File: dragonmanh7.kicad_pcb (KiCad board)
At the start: 4 copper layers, 135.6 x 54.6 mm, 109 parts, among them J1 USB_B, J10 Conn_02x12_Odd_Even, J11 Conn_02x03_Odd_Even, J12 VBAT+, J13 Conn_02x05_Odd_Even, J14 VBATG, J15 Conn_02x02_Odd_Even, J18 Conn_02x05_Odd_Even, J2 73725-0110BLF, J3 RJ45_Amphenol_RJMG1BD3B8K1ANR, J4 Micro_SD_Card, J5 Screw_Terminal_01x06, J6 Conn_02x12_Odd_Even, J7 USB_B, J8 Screw_Terminal_01x02, J9 Conn_02x12_Odd_Even, SW1 RESET, SW2 PC13, U1 STM32H743VITx, U10 USBLC6-2SC6, U11 SN6505, U12 TCAN332, U13 ISL83483, U14 MIC2005A, U2 KSZ8081RNA, U3 ISO1050DUB, U4 ISO3082DW, U5 S25FL127SABMFI101, U6 AP63203, U7 USBLC6-2SC6, U8 STM32F042F6Px, U9 USBLC6-2SC6, Y1 8MHz, Y2 32.768KHz, Y3 25MHz

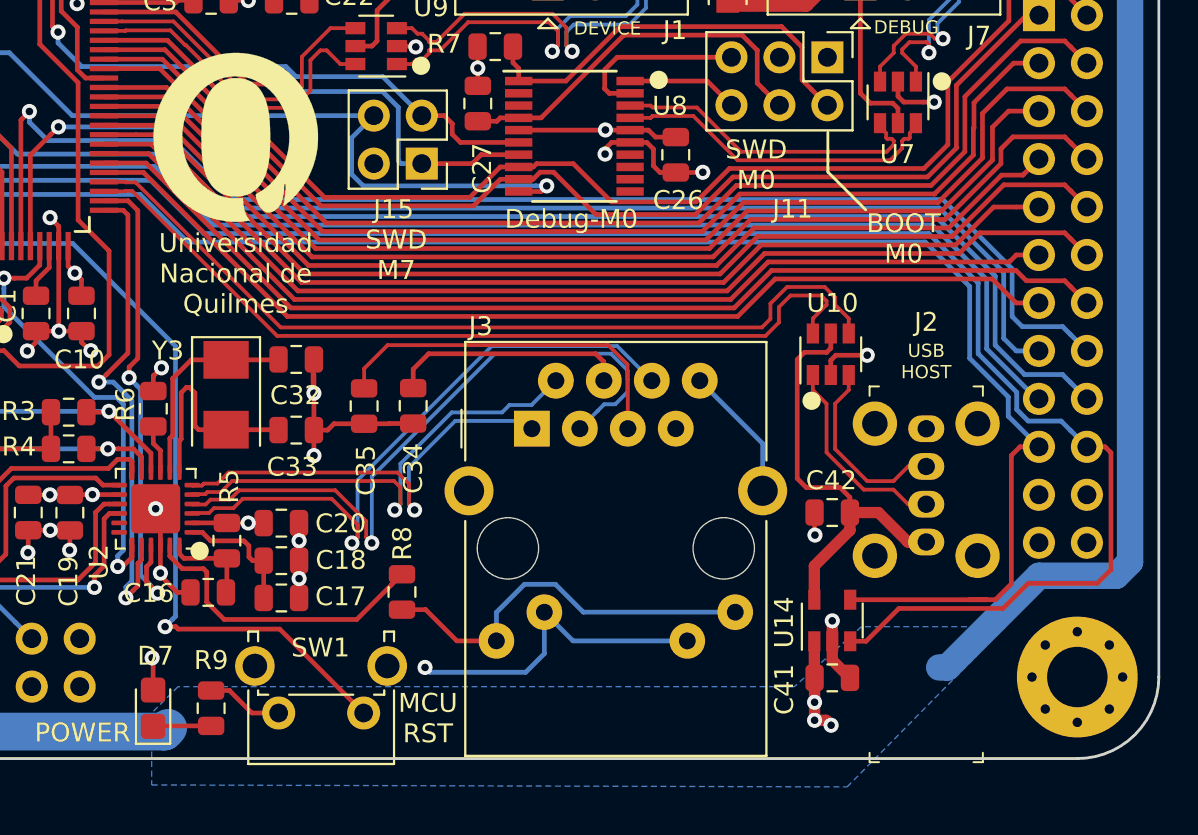
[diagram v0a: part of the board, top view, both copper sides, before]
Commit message: Reroute the power plane above RJ45 to prevent coupling
Signed-off-by: Martin Ribelotta <martinribelotta@gmail.com>
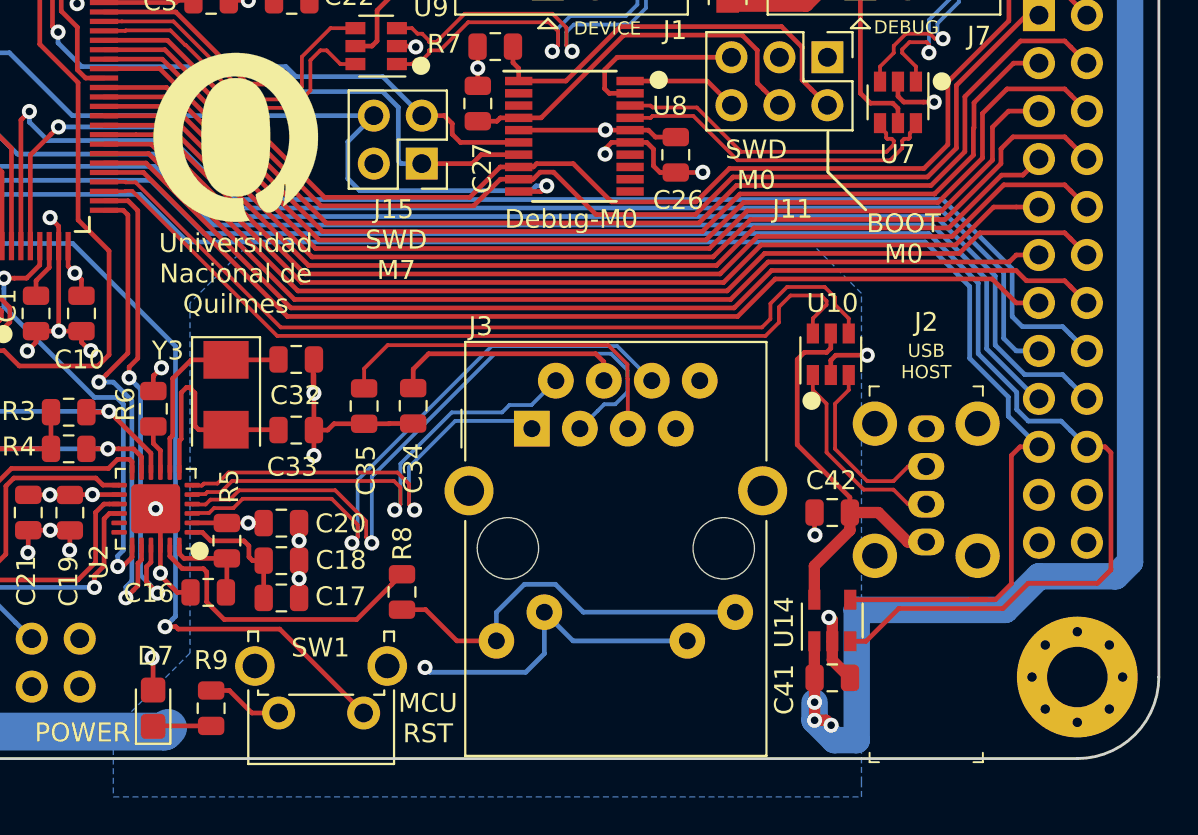
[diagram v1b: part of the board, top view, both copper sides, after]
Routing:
- net VDC: track 151.9 -> 165.6 mm
- net GND: track 178.7 -> 171.8 mm
- net /VBUS3: track 23.2 -> 22.2 mm
- net /~RESET: track 135.6 -> 136.2 mm
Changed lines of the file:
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@@
     (thickness 1.6)
     (drawings 76)
-    (tracks 2290)
+    (tracks 2293)
     (zones 0)
     (modules 109)
@@
   (segment (start 177.01514 77.33768) (end 177.95264 78.27518) (width 0.6) (layer F.Cu) (net 2))
   (segment (start 177.01514 76.33734) (end 177.01514 77.33768) (width 0.6) (layer F.Cu) (net 2))
-  (via (at 177.01514 75.25512) (size 0.8) (drill 0.4) (layers F.Cu B.Cu) (net 2))
-  (segment (start 177.01514 76.33734) (end 177.01514 75.25512) (width 0.6) (layer F.Cu) (net 2))
   (segment (start 109.22 33.0985) (end 109.22 33.02) (width 0.25) (layer F.Cu) (net 2))
   (segment (start 111.76 35.6385) (end 109.22 33.0985) (width 0.25) (layer F.Cu) (net 2))
@@
   (segment (start 163.28712 76.31734) (end 169.33712 76.31734) (width 0.25) (layer B.Cu) (net 2))
   (segment (start 161.76712 74.79734) (end 163.28712 76.31734) (width 0.25) (layer B.Cu) (net 2))
-  (segment (start 173.32712 65.86734) (end 173.32712 68.36734) (width 0.25) (layer B.Cu) (net 2))
-  (segment (start 169.99712 62.53734) (end 173.32712 65.86734) (width 0.25) (layer B.Cu) (net 2))
   (via (at 155.448 77.724) (size 0.8) (drill 0.4) (layers F.Cu B.Cu) (net 2))
   (segment (start 155.702 77.978) (end 155.448 77.724) (width 0.25) (layer B.Cu) (net 2))
@@
   (segment (start 150.28926 65.15354) (end 149.56306 65.15354) (width 0.25) (layer F.Cu) (net 2))
   (segment (start 150.6243 64.8185) (end 150.28926 65.15354) (width 0.25) (layer F.Cu) (net 2))
+  (segment (start 176.881544 75.073744) (end 176.833764 75.073744) (width 0.6) (layer F.Cu) (net 2))
+  (segment (start 177.01514 76.33734) (end 177.01514 75.20734) (width 0.6) (layer F.Cu) (net 2))
+  (via (at 176.833764 75.073744) (size 0.8) (drill 0.4) (layers F.Cu B.Cu) (net 2))
+  (segment (start 177.01514 75.20734) (end 176.881544 75.073744) (width 0.6) (layer F.Cu) (net 2))
   (segment (start 134.84606 57.245772) (end 134.84606 58.03876) (width 0.25) (layer F.Cu) (net 3))
   (segment (start 135.545281 55.410141) (end 135.545281 56.546551) (width 0.25) (layer F.Cu) (net 3))
@@
   (segment (start 125.73762 49.90592) (end 131.1021 55.2704) (width 0.25) (layer B.Cu) (net 33))
   (segment (start 160.40756 52.5185) (end 161.593396 52.5185) (width 0.25) (layer F.Cu) (net 33))
-  (segment (start 151.560279 51.605301) (end 152.174113 52.219135) (width 0.25) (layer B.Cu) (net 33))
   (via (at 161.892761 52.219135) (size 0.8) (drill 0.4) (layers F.Cu B.Cu) (net 33))
-  (segment (start 152.174113 52.219135) (end 161.327076 52.219135) (width 0.25) (layer B.Cu) (net 33))
   (segment (start 161.593396 52.5185) (end 161.892761 52.219135) (width 0.25) (layer F.Cu) (net 33))
-  (segment (start 151.560279 49.676301) (end 151.560279 51.605301) (width 0.25) (layer B.Cu) (net 33))
-  (segment (start 152.73528 48.5013) (end 151.560279 49.676301) (width 0.25) (layer B.Cu) (net 33))
   (segment (start 161.327076 52.219135) (end 161.892761 52.219135) (width 0.25) (layer B.Cu) (net 33))
+  (segment (start 161.069811 52.4764) (end 161.327076 52.219135) (width 0.25) (layer B.Cu) (net 33))
+  (segment (start 151.9936 52.4764) (end 161.069811 52.4764) (width 0.25) (layer B.Cu) (net 33))
+  (segment (start 151.3586 51.8414) (end 151.9936 52.4764) (width 0.25) (layer B.Cu) (net 33))
+  (segment (start 152.73528 48.5013) (end 151.3586 49.87798) (width 0.25) (layer B.Cu) (net 33))
+  (segment (start 151.3586 49.87798) (end 151.3586 51.8414) (width 0.25) (layer B.Cu) (net 33))
   (segment (start 130.19532 64.94018) (end 130.72364 64.41186) (width 0.25) (layer F.Cu) (net 34))
   (segment (start 129.667 64.94018) (end 130.19532 64.94018) (width 0.25) (layer F.Cu) (net 34))
@@
   (segment (start 107.739978 81.11998) (end 107.00766 80.387662) (width 2) (layer B.Cu) (net 46))
   (segment (start 105.239701 73.997701) (end 98.381701 73.997701) (width 2) (layer B.Cu) (net 46))
-  (segment (start 184.404 40.132) (end 180.90642 36.63442) (width 1.4) (layer B.Cu) (net 46))
-  (segment (start 183.1086 77.724) (end 187.962599 72.870001) (width 1.4) (layer B.Cu) (net 46))
-  (segment (start 182.6768 77.724) (end 183.1086 77.724) (width 1.4) (layer B.Cu) (net 46))
+  (segment (start 176.07764 79.56828) (end 176.07764 80.52284) (width 1.4) (layer B.Cu) (net 46))
   (segment (start 191.77 40.132) (end 184.404 40.132) (width 1.4) (layer B.Cu) (net 46))
+  (segment (start 184.404 40.132) (end 180.90642 36.63442) (width 1.4) (layer B.Cu) (net 46))
   (segment (start 192.786 41.148) (end 191.77 40.132) (width 1.4) (layer B.Cu) (net 46))
   (segment (start 192.786 72.136) (end 192.786 41.148) (width 1.4) (layer B.Cu) (net 46))
-  (segment (start 187.962599 72.870001) (end 192.051999 72.870001) (width 1.4) (layer B.Cu) (net 46))
-  (segment (start 192.051999 72.870001) (end 192.786 72.136) (width 1.4) (layer B.Cu) (net 46))
+  (segment (start 192.024 72.898) (end 192.786 72.136) (width 1.4) (layer B.Cu) (net 46))
+  (segment (start 178.308 74.676) (end 186.182 74.676) (width 1.4) (layer B.Cu) (net 46))
+  (segment (start 177.12979 81.57499) (end 178.308 81.57499) (width 1.4) (layer B.Cu) (net 46))
+  (segment (start 176.07764 80.52284) (end 177.12979 81.57499) (width 1.4) (layer B.Cu) (net 46))
+  (segment (start 178.308 81.57499) (end 178.308 74.676) (width 1.4) (layer B.Cu) (net 46))
+  (segment (start 186.182 74.676) (end 187.96 72.898) (width 1.4) (layer B.Cu) (net 46))
+  (segment (start 187.96 72.898) (end 192.024 72.898) (width 1.4) (layer B.Cu) (net 46))
   (segment (start 72.92848 70.83552) (end 73.05954 70.83552) (width 1) (layer F.Cu) (net 47))
   (segment (start 70.60184 74.59182) (end 70.60184 73.16216) (width 1) (layer F.Cu) (net 47))
@@
   (segment (start 176.06514 72.34686) (end 177.9501 70.4619) (width 0.6) (layer F.Cu) (net 62))
   (segment (start 176.9364 60.8178) (end 176.9364 60.0378) (width 0.25) (layer F.Cu) (net 62))
-  (segment (start 175.5394 61.0362) (end 176.718 61.0362) (width 0.25) (layer F.Cu) (net 62))
-  (segment (start 177.9501 69.5198) (end 177.9501 68.7198) (width 0.25) (layer F.Cu) (net 62))
-  (segment (start 177.4293 68.199) (end 175.641 68.199) (width 0.25) (layer F.Cu) (net 62))
-  (segment (start 177.9501 68.7198) (end 177.4293 68.199) (width 0.25) (layer F.Cu) (net 62))
-  (segment (start 175.1584 67.7164) (end 175.1584 61.4172) (width 0.25) (layer F.Cu) (net 62))
   (segment (start 176.718 61.0362) (end 176.9364 60.8178) (width 0.25) (layer F.Cu) (net 62))
-  (segment (start 175.641 68.199) (end 175.1584 67.7164) (width 0.25) (layer F.Cu) (net 62))
+  (segment (start 177.9501 69.5198) (end 177.9501 68.7198) (width 0.25) (layer F.Cu) (net 62))
+  (segment (start 175.1584 65.9281) (end 175.1584 61.4172) (width 0.25) (layer F.Cu) (net 62))
   (segment (start 175.1584 61.4172) (end 175.5394 61.0362) (width 0.25) (layer F.Cu) (net 62))
+  (segment (start 177.9501 68.7198) (end 175.1584 65.9281) (width 0.25) (layer F.Cu) (net 62))
+  (segment (start 175.5394 61.0362) (end 176.718 61.0362) (width 0.25) (layer F.Cu) (net 62))
   (segment (start 180.49494 48.11772) (end 180.21812 47.8409) (width 0.25) (layer F.Cu) (net 63))
   (segment (start 180.49494 48.89772) (end 180.49494 48.11772) (width 0.25) (layer F.Cu) (net 63))
@@
     )
   )
-  (zone (net 46) (net_name VDC) (layer B.Cu) (hatch edge 0.508)
-    (connect_pads (clearance 0.254))
-    (min_thickness 0.254)
-    (fill yes (arc_segments 16) (thermal_gap 0.508) (thermal_bridge_width 0.508))
-    (polygon
-      (pts
-        (xy 140.972535 83.947) (xy 177.8 84.05114) (xy 186.182 75.565) (xy 178.562 75.565) (xy 175.006 78.74)
-        (xy 142.367 78.74) (xy 140.97 80.137)
-      )
-    )
-  )
   (zone (net 123) (net_name GNDPWR) (layer B.Cu) (hatch edge 0.508)
     (priority 1)
@@
     (polygon
       (pts
-        (xy 157.734 60.452) (xy 157.734 85.344) (xy 173.228 85.344) (xy 173.228 60.452)
+        (xy 157.734 66.802) (xy 157.734 85.344) (xy 173.228 85.344) (xy 173.228 66.802)
+      )
+    )
+  )
+  (zone (net 46) (net_name VDC) (layer B.Cu) (hatch edge 0.508)
+    (connect_pads (clearance 0.254))
+    (min_thickness 0.254)
+    (fill yes (arc_segments 32) (thermal_gap 0.254) (thermal_bridge_width 0.508))
+    (polygon
+      (pts
+        (xy 178.562 83.82) (xy 178.562 57.912) (xy 175.768 55.118) (xy 146.304 55.118) (xy 143.002 58.42)
+        (xy 143.002 76.962) (xy 138.938 81.026) (xy 138.938 84.582) (xy 178.562 84.582)
+      )
+    )
+  )
+  (zone (net 0) (net_name "") (layer B.Cu) (hatch edge 0.508)
+    (connect_pads (clearance 1))
+    (min_thickness 0.254)
+    (keepout (tracks allowed) (vias allowed) (copperpour not_allowed))
+    (fill (arc_segments 32) (thermal_gap 0.508) (thermal_bridge_width 0.508))
+    (polygon
+      (pts
+        (xy 151.13 84.582) (xy 151.13 66.802) (xy 158.496 59.436) (xy 174.244 59.436) (xy 175.006 60.198)
+        (xy 175.006 84.582)
       )
     )

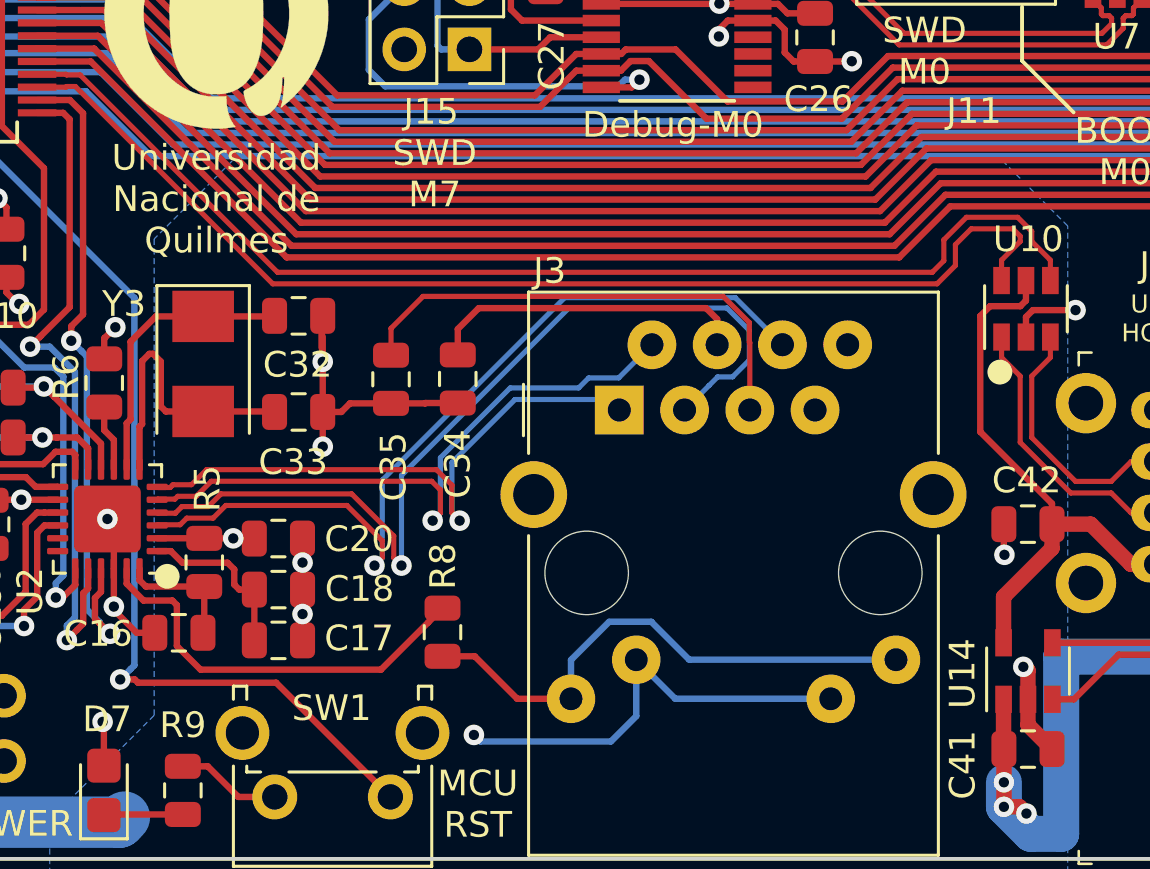
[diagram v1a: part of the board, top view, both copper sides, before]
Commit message: Improve ethernet connections (impedance matching TODO)
Signed-off-by: Martin Ribelotta <martinribelotta@gmail.com>
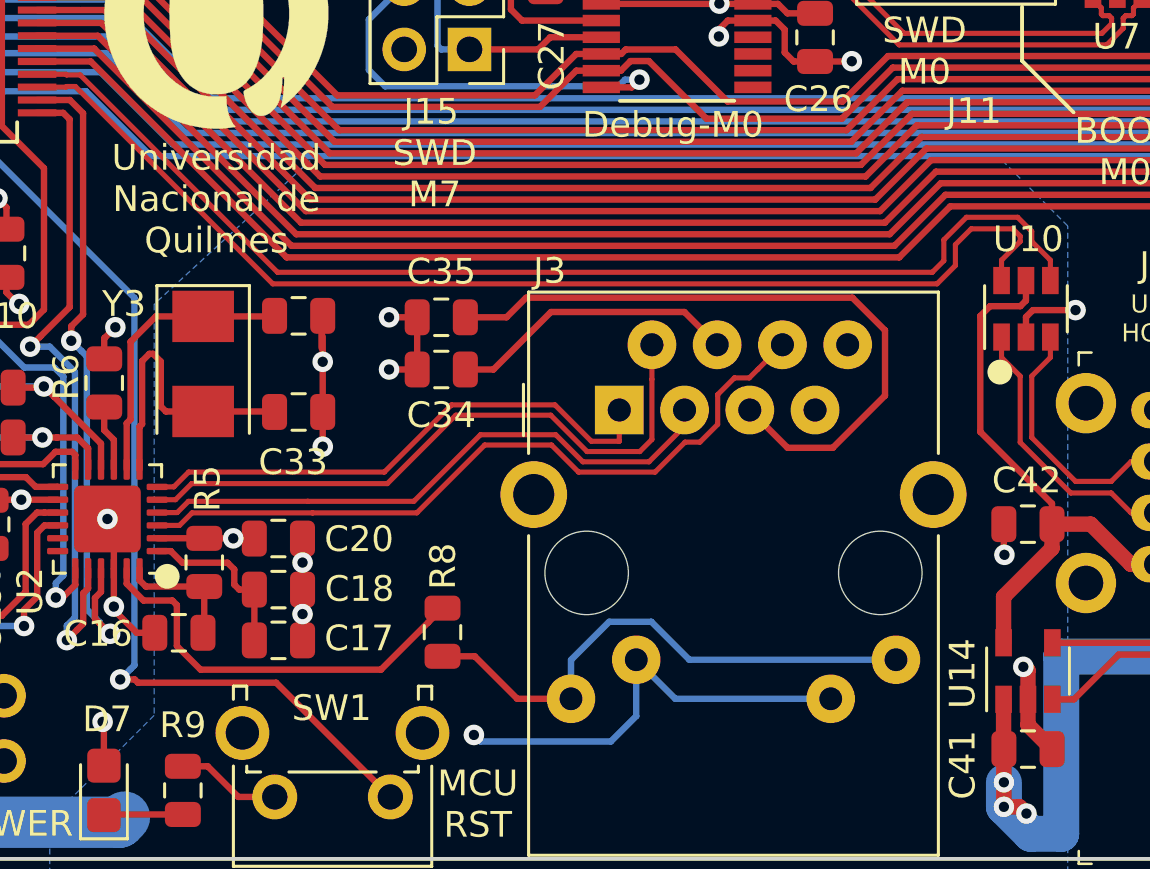
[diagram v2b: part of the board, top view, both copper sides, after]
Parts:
- moved C35 3.11 mm to (154.2, 61.5), turned to 0 degrees
- moved C34 0.74 mm to (154.2, 63.5), turned to 0 degrees
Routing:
- net /RD+: track 36.1 -> 23.4 mm, vias 1 -> 0
- net Net-(C35-Pad2): track 19.3 -> 26.4 mm
- net /RD-: track 33.5 -> 28.8 mm, vias 1 -> 0
- net /TD+: track 23.6 -> 21.1 mm, vias 1 -> 0
- net Net-(C34-Pad2): track 12.6 -> 11.3 mm
- net GND: track 171.8 -> 170.6 mm, vias 58 -> 60
- net /TD-: track 25.4 -> 25.1 mm, vias 1 -> 0

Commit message: Impreove some traces
Signed-off-by: Martin Ribelotta <martinribelotta@gmail.com>
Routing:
- net /USBD_D-: track 17.5 -> 14.9 mm
- net /USBD_D+: track 17.5 -> 14.9 mm
- net /~RESET: track 136.2 -> 134.3 mm
- net /U1_RX: track 65.1 -> 67.0 mm
- net /U1_TX: track 60.9 -> 62.4 mm
